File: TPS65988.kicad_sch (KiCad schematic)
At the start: 65 parts

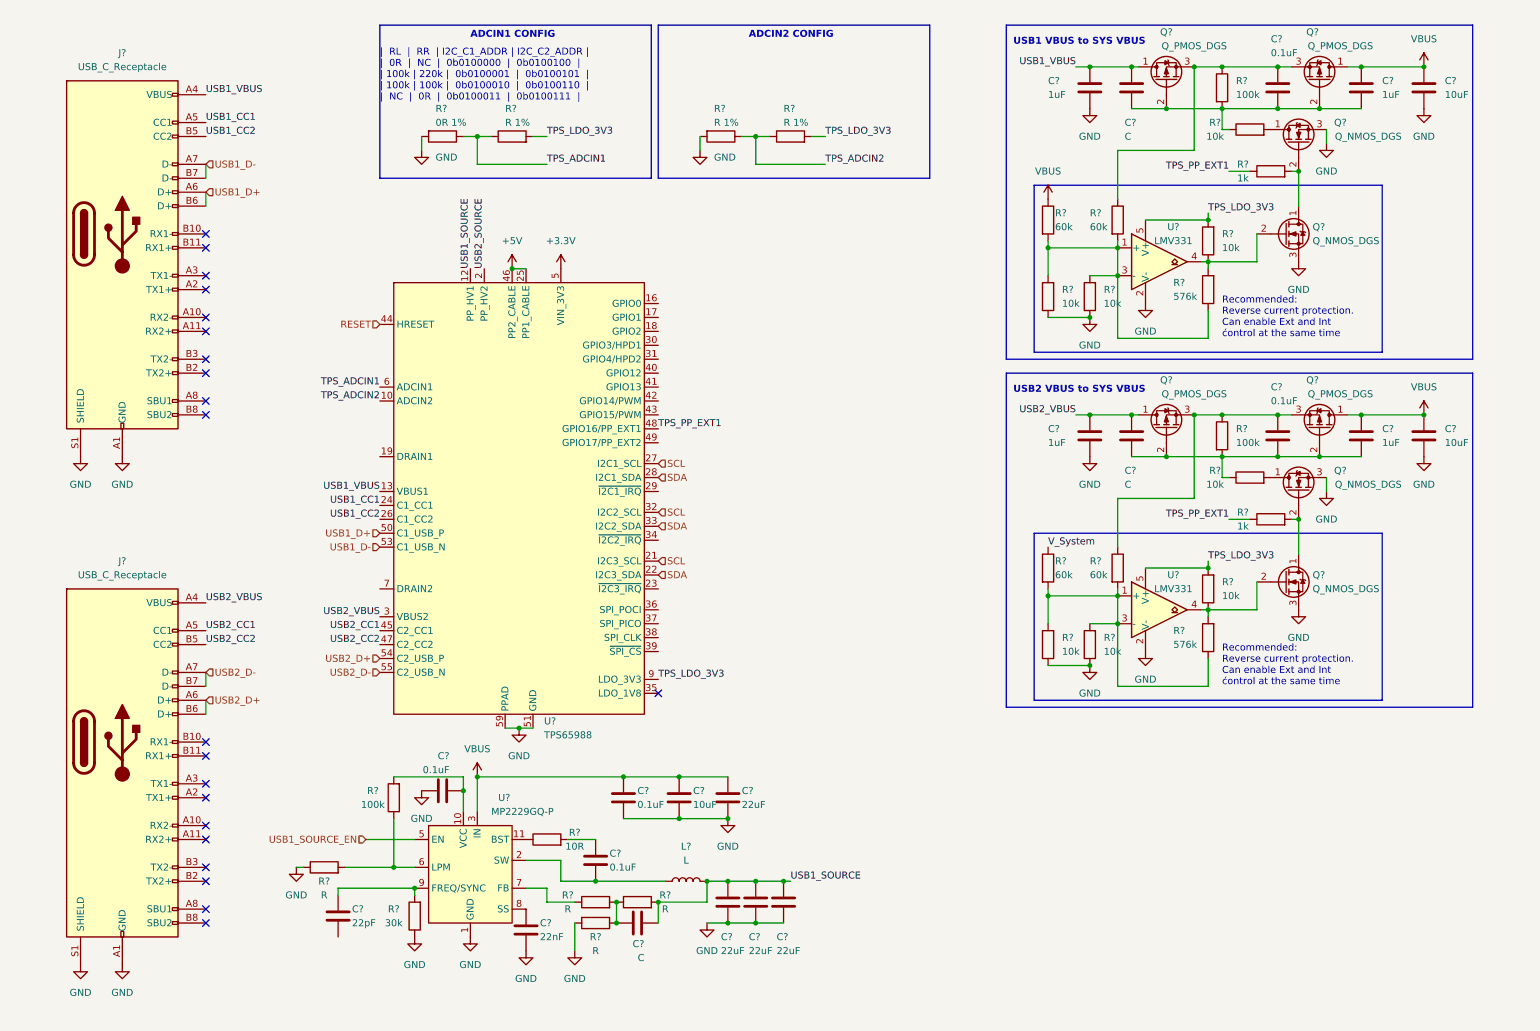
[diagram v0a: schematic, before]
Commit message: added digi-pote symbol, added USB_source voltage regulators
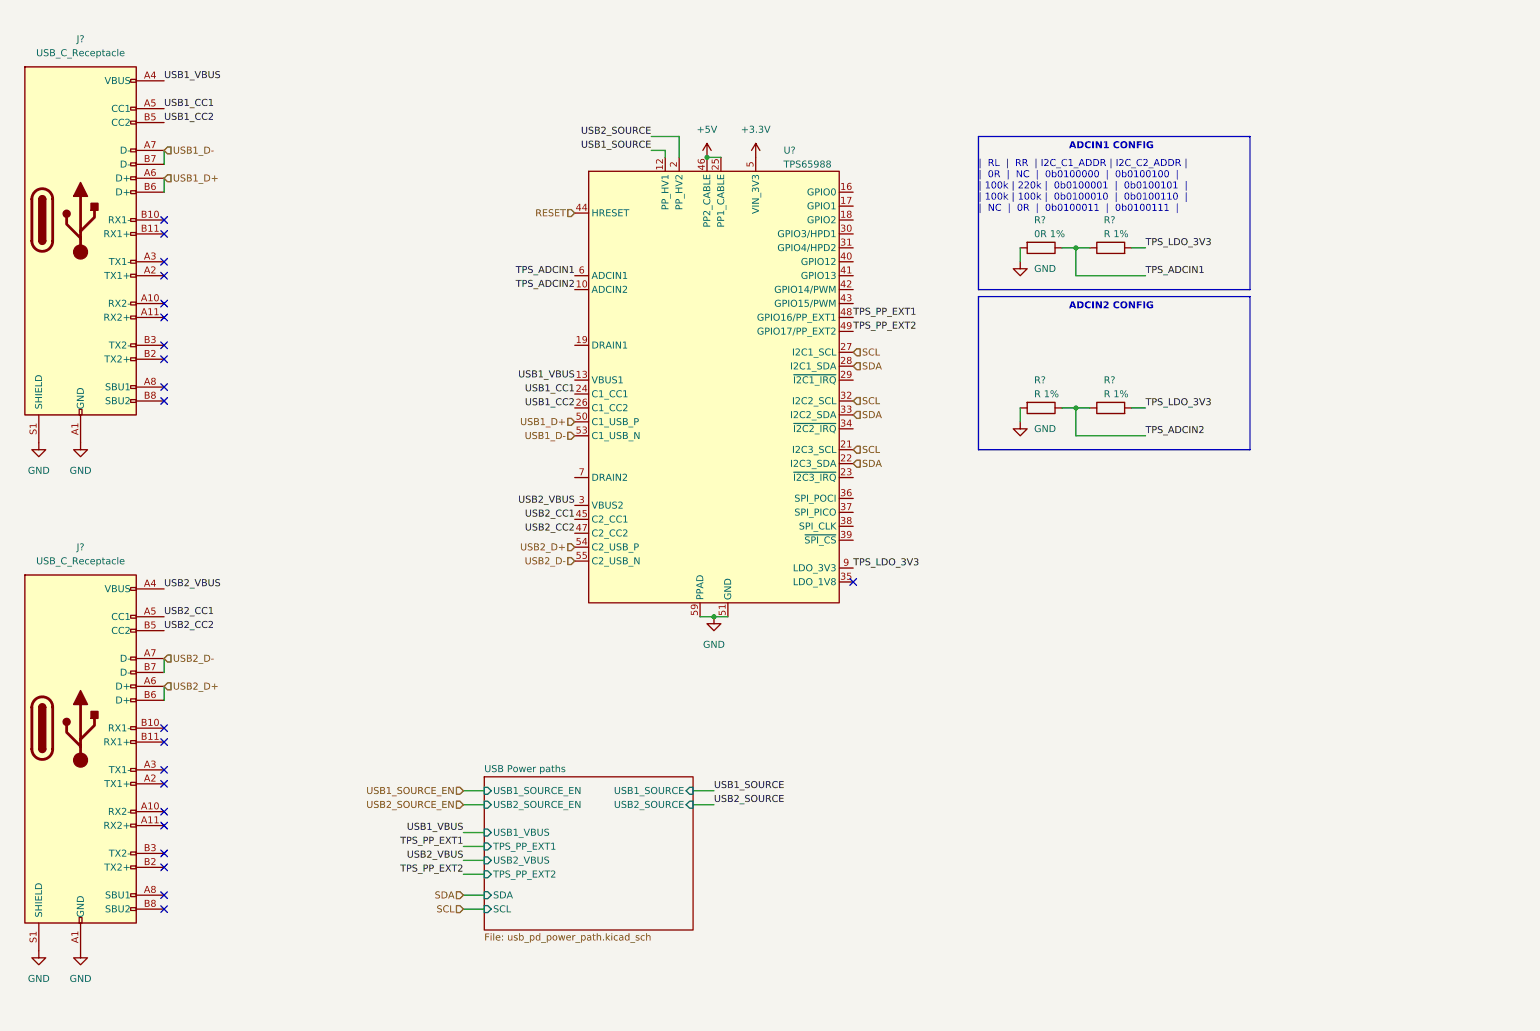
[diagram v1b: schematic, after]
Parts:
- removed C? (x3): C, symbol Device:C
- removed C? (x4): 1uF, symbol Device:C
- removed C? (x3): 10uF, symbol Device:C
- removed C?: 22nF, symbol Device:C
- removed C?: 22pF, symbol Device:C
- removed C? (x4): 22uF, symbol Device:C
- removed C? (x5): 0.1uF, symbol Device:C
- removed L?: L, symbol Device:L
- removed Q? (x4): Q_NMOS_DGS, symbol Device:Q_NMOS_DGS
- removed Q? (x4): Q_PMOS_DGS, symbol Device:Q_PMOS_DGS
- removed R? (x4): 60k, symbol Device:R
- removed R? (x8): 10k, symbol Device:R
- removed R? (x3): 100k, symbol Device:R
- removed R? (x4): R, symbol Device:R
- removed R? (x2): 1k, symbol Device:R
- removed R?: 30k, symbol Device:R
- removed R?: 10R, symbol Device:R
- removed R? (x2): 576k, symbol Device:R
- removed U? (x2): LMV331, symbol Comparator:LMV331
- removed U?: MP2229GQ-P, symbol airsoft_controller:MP2229GQ-P
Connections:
- net TPS_PP_EXT2: now reaches U?.49 (GPIO17/PP_EXT2)
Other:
- added sheet USB Power paths (usb_pd_power_path.kicad_sch)
- note removed: "Recommended: Reverse current protection. Can enable Ext and Int ćontrol at the same time"
- note removed: "USB1 VBUS to SYS VBUS"
- note removed: "USB2 VBUS to SYS VBUS"
- moved on the sheet: J?, R?, U?

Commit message: added audio ref schematic, added bat to 5V, added shift register, connected devices with other periferals
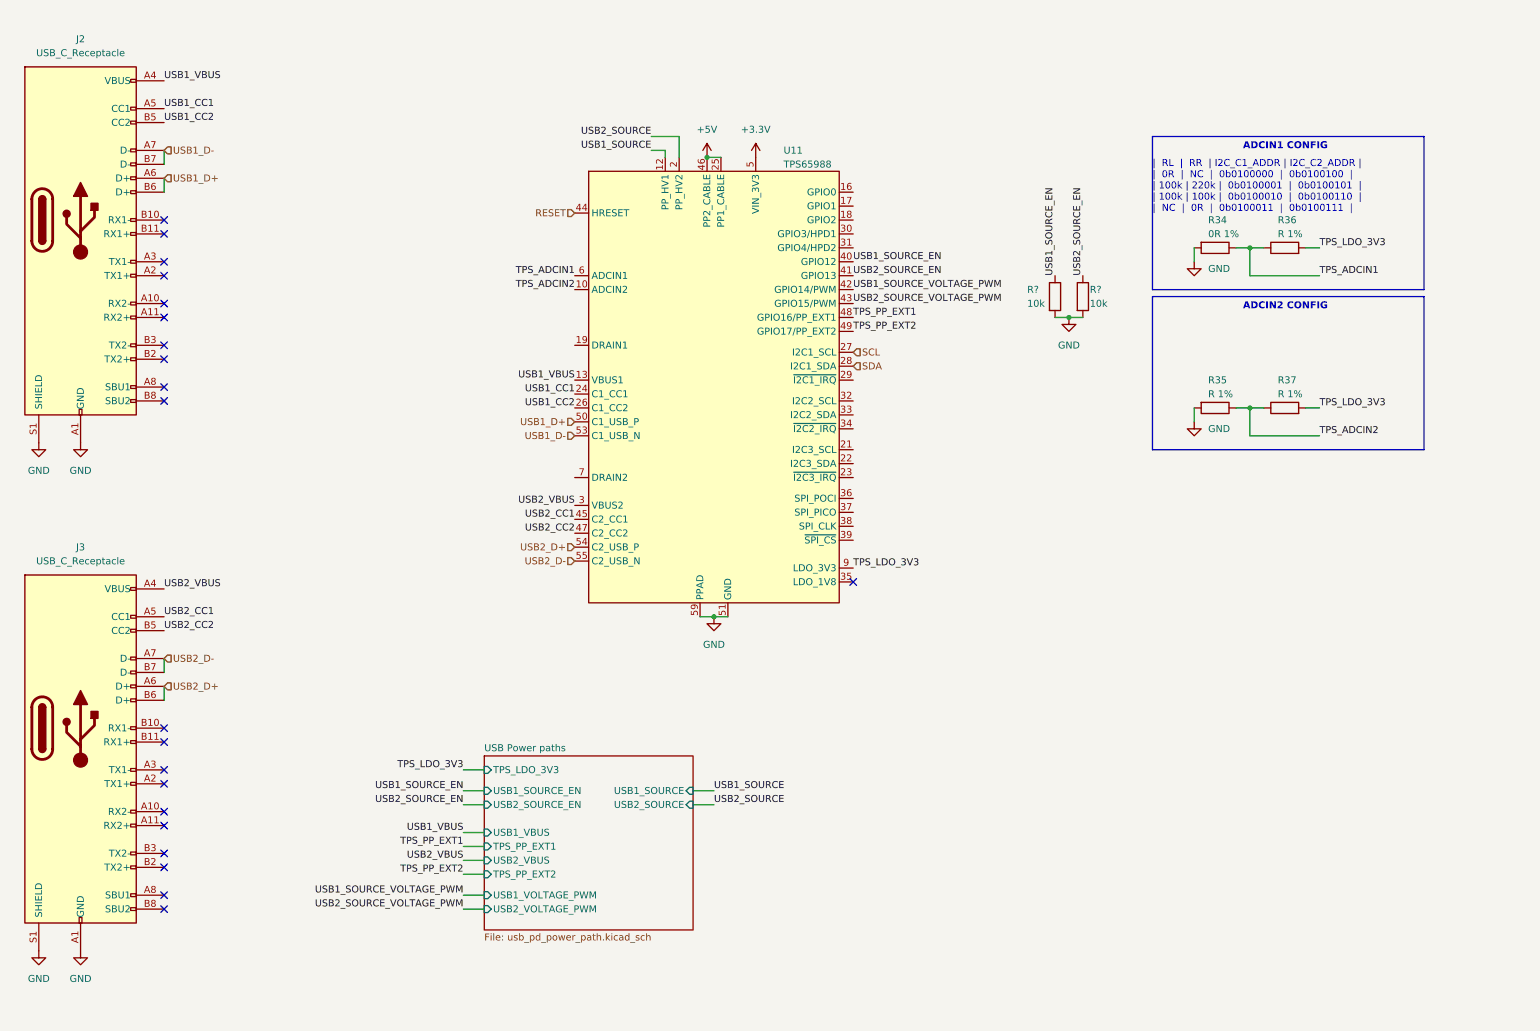
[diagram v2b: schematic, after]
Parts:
- added R? (x2): 10k, symbol Device:R
- gave numbers to parts that had none: 7
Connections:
- net GND: now also R?.2, R?.2
- net SCL: no longer U11.21 (I2C3_SCL), U11.32 (I2C2_SCL)
- net SDA: no longer U11.22 (I2C3_SDA), U11.33 (I2C2_SDA)
- net USB1_SOURCE_EN: now also U11.40 (GPIO12), R?.1
- net USB2_SOURCE_EN: now also U11.41 (GPIO13), R?.1
- net USB1_SOURCE_VOLTAGE_PWM: now reaches U11.42 (GPIO14/PWM)
- net USB2_SOURCE_VOLTAGE_PWM: now reaches U11.43 (GPIO15/PWM)
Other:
- sheet USB Power paths ports: added TPS_LDO_3V3, USB1_VOLTAGE_PWM, USB2_VOLTAGE_PWM; removed SCL, SDA
- moved on the sheet: R34, R35, R36, R37

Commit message: fixes
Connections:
- net TPS_ADCIN1: now also R35.1, R37.1; no longer R34.1, R36.1
- net TPS_ADCIN2: now also R34.1, R36.1; no longer R35.1, R37.1
- no-connect marks 21 -> 30
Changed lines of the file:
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@@
   (junction (at 139.7 39.37) (diameter 0) (color 0 0 0 0)
   )
+  (no_connect (at 115.57 73.66))
+  (no_connect (at 115.57 97.79))
+  (no_connect (at 132.08 96.52))
+  (no_connect (at 166.37 83.82))
+  (no_connect (at 166.37 86.36))
+  (no_connect (at 166.37 88.9))
+  (no_connect (at 166.37 92.71))
+  (no_connect (at 166.37 95.25))
+  (no_connect (at 166.37 97.79))
   (no_connect (at 40.64 83.82))
   (no_connect (at 40.64 76.2))
@@
     (effects (font (size 1.27 1.27)) (justify left bottom))
   )
-  (text "ADCIN1 CONFIG" (at 237.49 38.1 0)
+  (text "ADCIN2 CONFIG" (at 237.49 38.1 0)
     (effects (font (size 1.27 1.27) (thickness 0.254) bold) (justify left bottom))
   )
-  (text "ADCIN2 CONFIG" (at 237.49 67.31 0)
+  (text "ADCIN1 CONFIG" (at 237.49 67.31 0)
     (effects (font (size 1.27 1.27) (thickness 0.254) bold) (justify left bottom))
   )
@@
     (effects (font (size 1.27 1.27)) (justify right bottom))
   )
-  (label "TPS_ADCIN2" (at 251.46 90.17 0)
+  (label "TPS_ADCIN2" (at 251.46 60.96 0)
     (effects (font (size 1.27 1.27)) (justify left bottom))
   )
@@
     (effects (font (size 1.27 1.27)) (justify right bottom))
   )
-  (label "TPS_ADCIN1" (at 251.46 60.96 0)
-    (effects (font (size 1.27 1.27)) (justify left bottom))
-  )
+  (label "TPS_ADCIN1" (at 251.46 90.17 0)
+    (effects (font (size 1.27 1.27)) (justify left bottom))
+  )

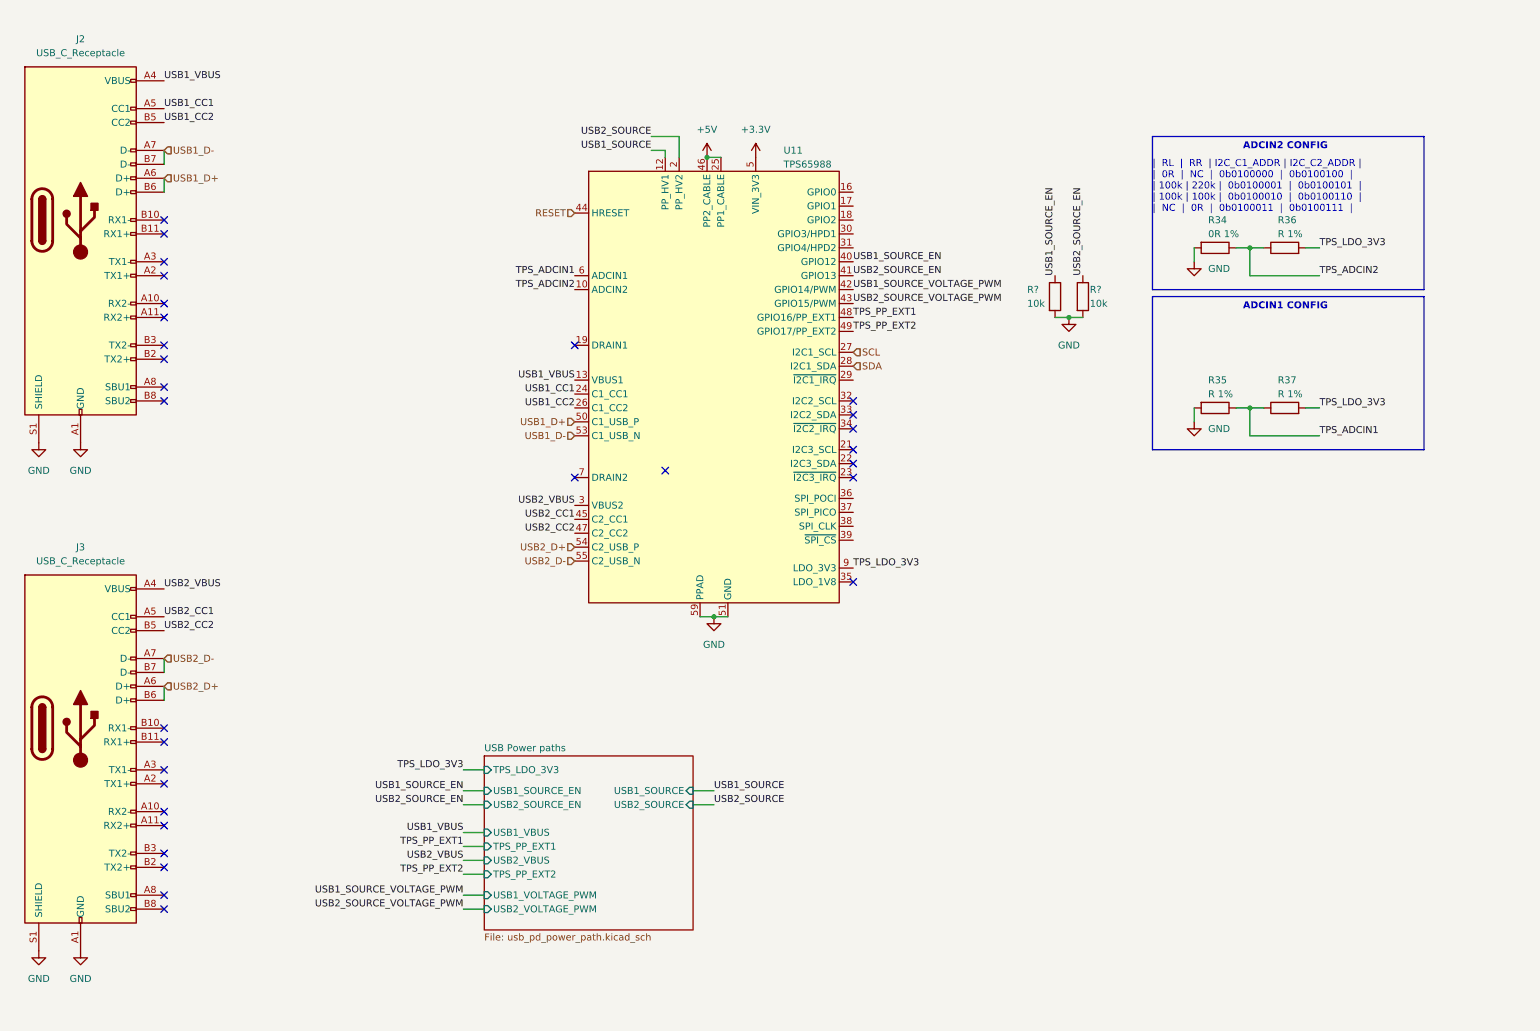
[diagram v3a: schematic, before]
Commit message: added adcin2 config description, fixed some rule check errors
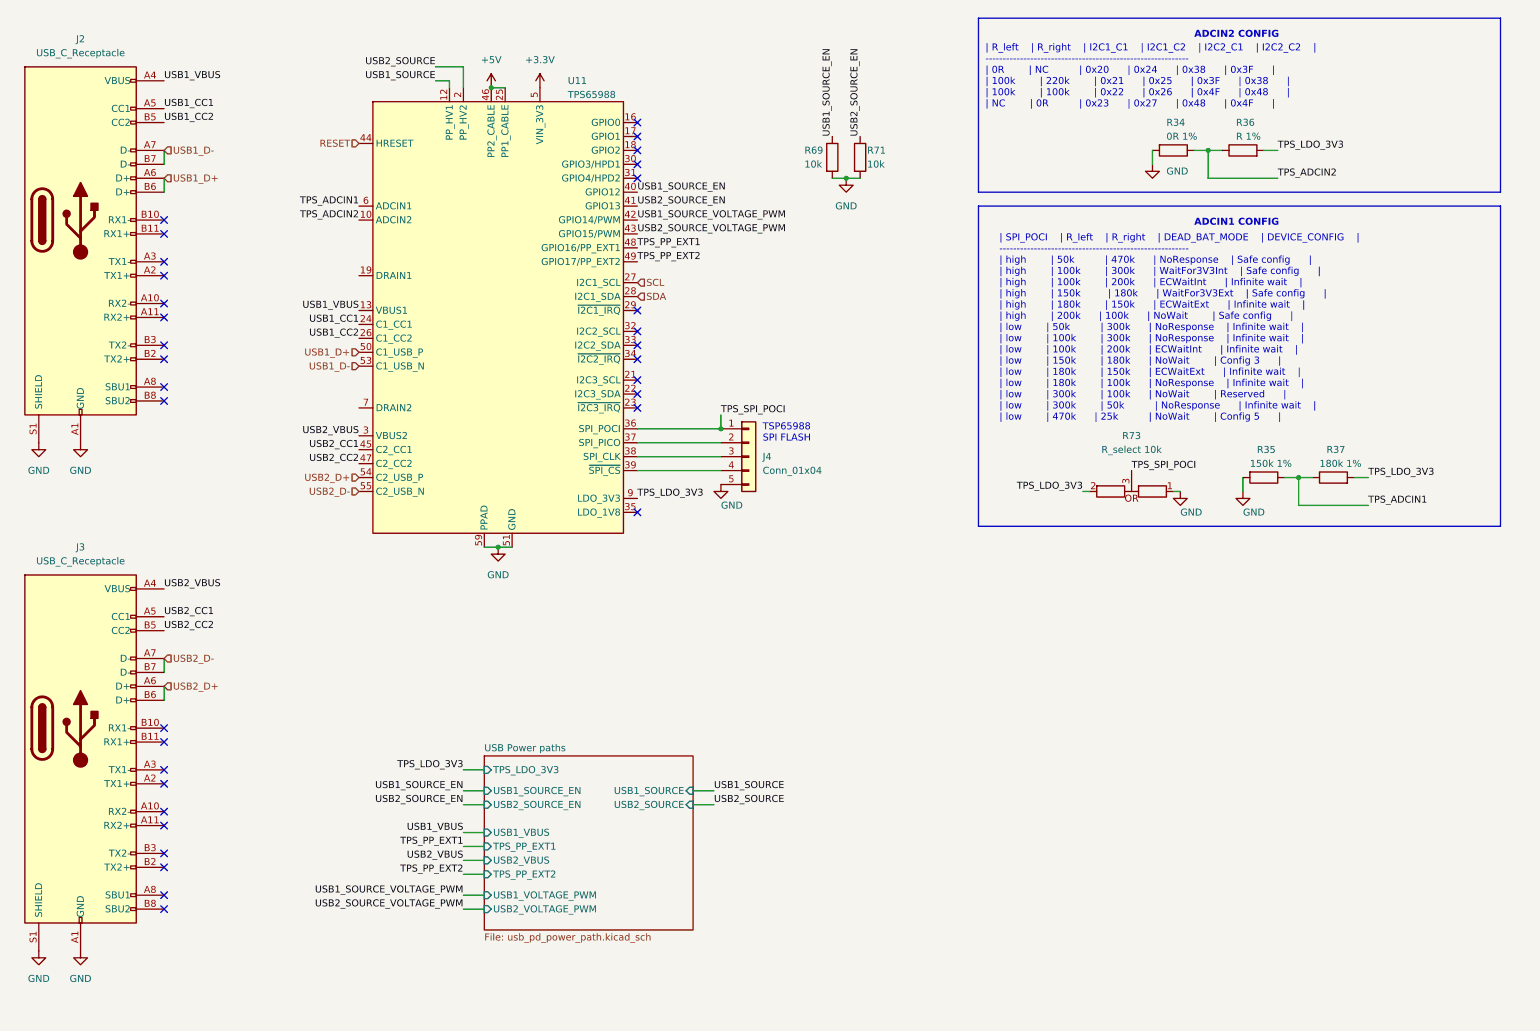
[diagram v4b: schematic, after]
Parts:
- added J4: Conn_01x04, symbol Connector_Generic:Conn_01x05
- added R73: R_select 10k, symbol airsoft_controller:R_select
- R35: value R 1% -> 150k 1%
- R37: value R 1% -> 180k 1%
- gave numbers to parts that had none: 2
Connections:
- net GND: now also J4.5 (Pin_5), R73.1
- net TPS_LDO_3V3: now also R73.2
- net TPS_SPI_POCI: now reaches U11.36 (SPI_POCI)
- net TPS_SPI_POCI: now also J4.1 (Pin_1), R73.3
- net at U11.37 (SPI_PICO): now also J4.2 (Pin_2)
- net at U11.38 (SPI_CLK): now also J4.3 (Pin_3)
- net at U11.39 (~{SPI_CS}): now also J4.4 (Pin_4)
- no-connect marks 30 -> 33
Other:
- note added: "TSP65988 SPI FLASH"
- note added: "| R_left | R_right | I2C1_C1 | I2C1_C2 | I2C2_C1 | I2C2_C2 | ----------------------------------------------------------- | 0R | NC | 0x20 | 0x24 | 0x38 | 0x3F | | 100k | 220k | 0x21 | 0x25 | 0x3F | 0x38 | | 100k | 100k | 0x22 | 0x26 | 0x4F | 0x48 | | NC | 0R | 0x23 | 0x27 | 0x48 | 0x4F |"
- note added: "| SPI_POCI | R_left | R_right | DEAD_BAT_MODE | DEVICE_CONFIG | ------------------------------------------------------- | high | 50k | 470k | NoResponse | Safe config | | high | 100k | 300k | WaitFor3V3Int | Safe config | | high | 100k | 200k | ECWaitInt | Infinite wait | | high | 150k | 180k | WaitFor3V3Ext | Safe config | | high | 180k | 150k | ECWaitExt | Infinite wait | | high | 200k | 100k |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"
- note removed: "| RL | RR | I2C_C1_ADDR | I2C_C2_ADDR | | 0R | NC | 0b0100000 | 0b0100100 | | 100k | 220k | 0b0100001 | 0b0100101 | | 100k | 100k | 0b0100010 | 0b0100110 | | NC | 0R | 0b0100011 | 0b0100111 |"
- moved on the sheet: R34, R35, R36, R37, R69, R71, U11
